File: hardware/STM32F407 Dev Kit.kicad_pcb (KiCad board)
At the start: 4 copper layers, 65.2 x 58.4 mm, 153 parts, among them J1 GMSB0531112YEU, J10 Conn_01x04, J11 TBC 2.54mm 10A, J12 IMP34DT05, J2 Conn_01x06, J3 RJMG1S8008101BR, J4 B2B-XH-A(LF)(SN), J5 Conn_01x04, J7 SJ-3524-SMT, J8 GMSB0531112YEU, J9 Conn_01x04, SW1 SW TACT-SPST, SW2 SW TACT-SPST, SW3 SW TACT-SPST, U1 STM32F103CBT6, U2 DP83826IRHBR, U3 DRV8701ERGET, U4 DMHT6016LFJ-13, U5 ADS122C04IPW, U6 CS43L22, U7 STM32F407VGT6, U8 AP63203WU, U9 XC6206P182MR, Y1 ABM8G-8.000MHZ-18-D2Y-T, Y2 ABM8G-25.000MHZ-9-B4Y-T, Y3 ABM8G-8.000MHZ-18-D2Y-T

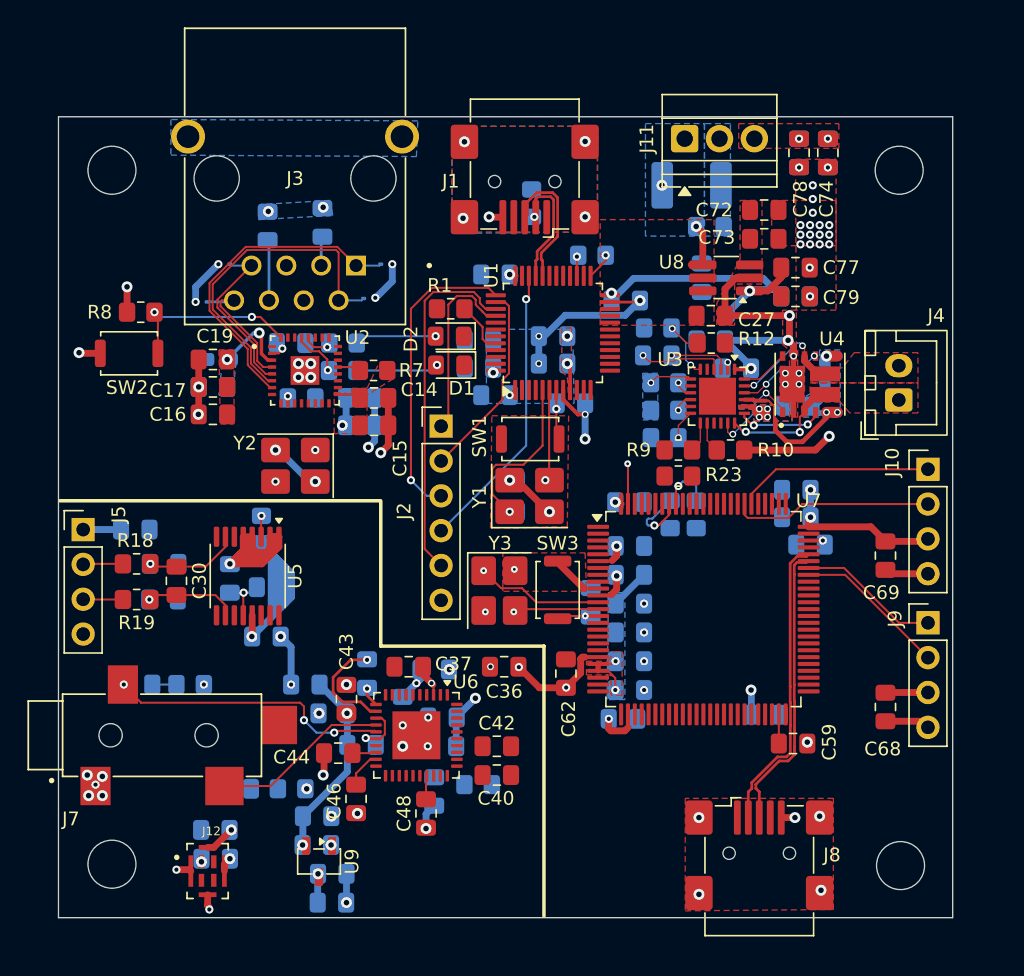
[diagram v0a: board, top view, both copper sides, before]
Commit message: Route Ethernet connections to STM32F407
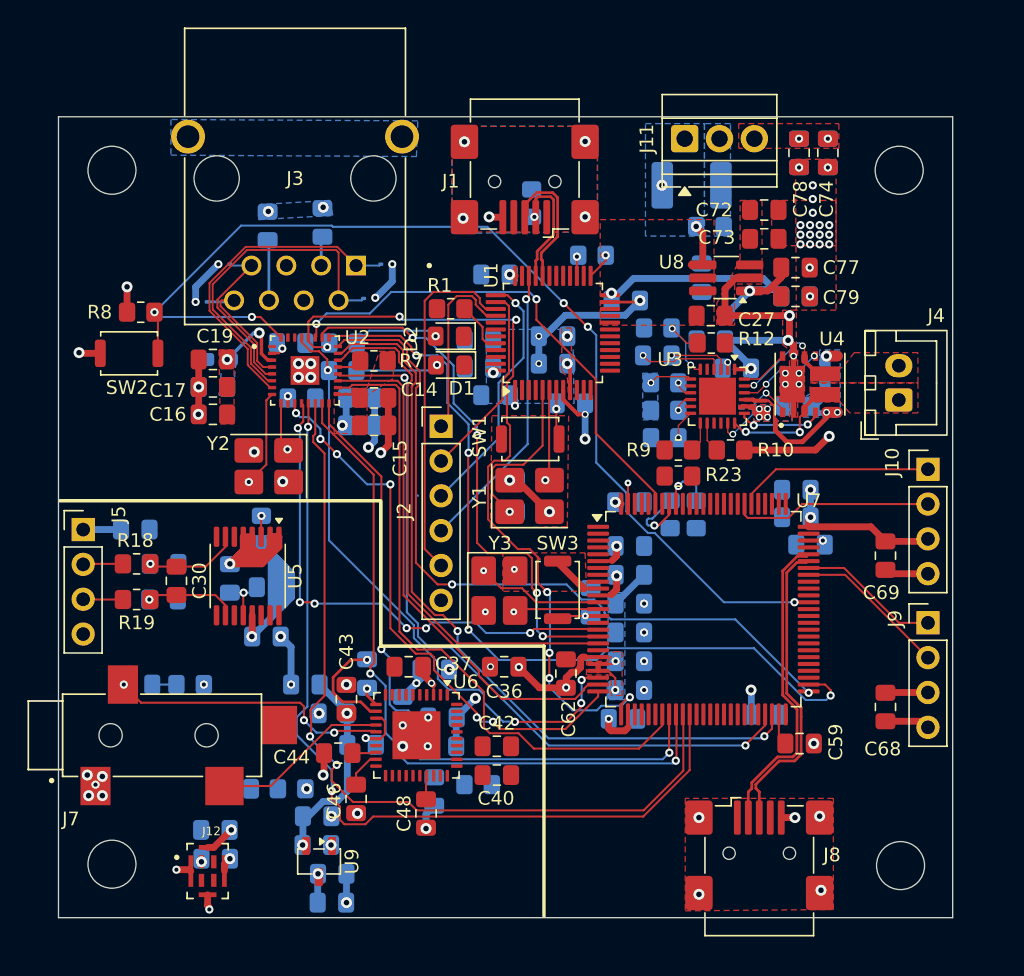
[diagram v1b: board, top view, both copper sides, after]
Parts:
- moved C20 1.95 mm to (165.3, 74.4)
- moved Y2 1.95 mm to (165.3, 75.5)
- moved C21 1.93 mm to (165.3, 76.6)
- moved R7 0.70 mm to (173.0, 67.8)
- moved C59 0.47 mm to (204.0, 95.7)
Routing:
- net PHY_NRST: track 13.1 -> 81.0 mm, vias 2 -> 5
- net RX_D3: track 0.00 -> 63.4 mm, vias 0 -> 2
- net TX_D1: track 0.00 -> 61.2 mm, vias 0 -> 4
- net RX_D2: track 0.00 -> 61.2 mm, vias 0 -> 2
- net COL: track 2.20 -> 58.3 mm, vias 1 -> 7
- net TX_EN: track 0.00 -> 56.1 mm, vias 0 -> 2
- net TX_D0: track 0.00 -> 54.3 mm, vias 0 -> 2
- net RX_ER: track 0.00 -> 54.3 mm, vias 0 -> 2
- net RX_D1: track 0.00 -> 52.4 mm, vias 0 -> 2
- net RX_D0: track 0.00 -> 50.4 mm, vias 0 -> 2
- net RX_DV: track 0.00 -> 48.1 mm
- net CRS: track 3.52 -> 45.1 mm, vias 1 -> 4
- net MDIO: track 0.00 -> 41.0 mm, vias 0 -> 6
- net TX_D2: track 0.00 -> 39.3 mm, vias 0 -> 4
- net TX_CLK: track 0.00 -> 38.5 mm
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
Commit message: Route debugger connections to STM32F407
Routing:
- net F407_JTMS: track 1.54 -> 57.7 mm, vias 1 -> 3
- net F407_JTCLK: track 0.00 -> 50.6 mm, vias 0 -> 2
- net F407_NTRST: track 3.97 -> 27.3 mm, vias 1 -> 3
- net GND: vias 100 -> 99

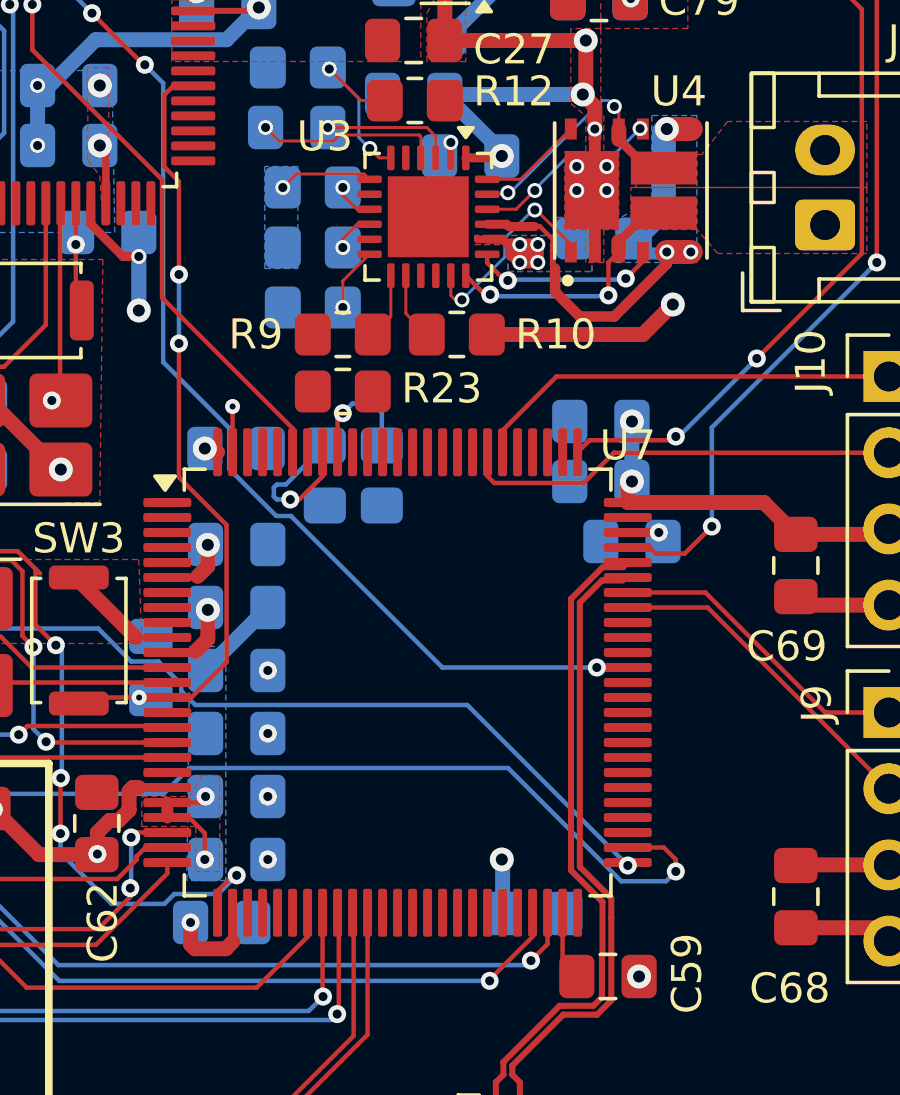
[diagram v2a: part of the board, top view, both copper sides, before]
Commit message: Route Motor connections to STM32F407
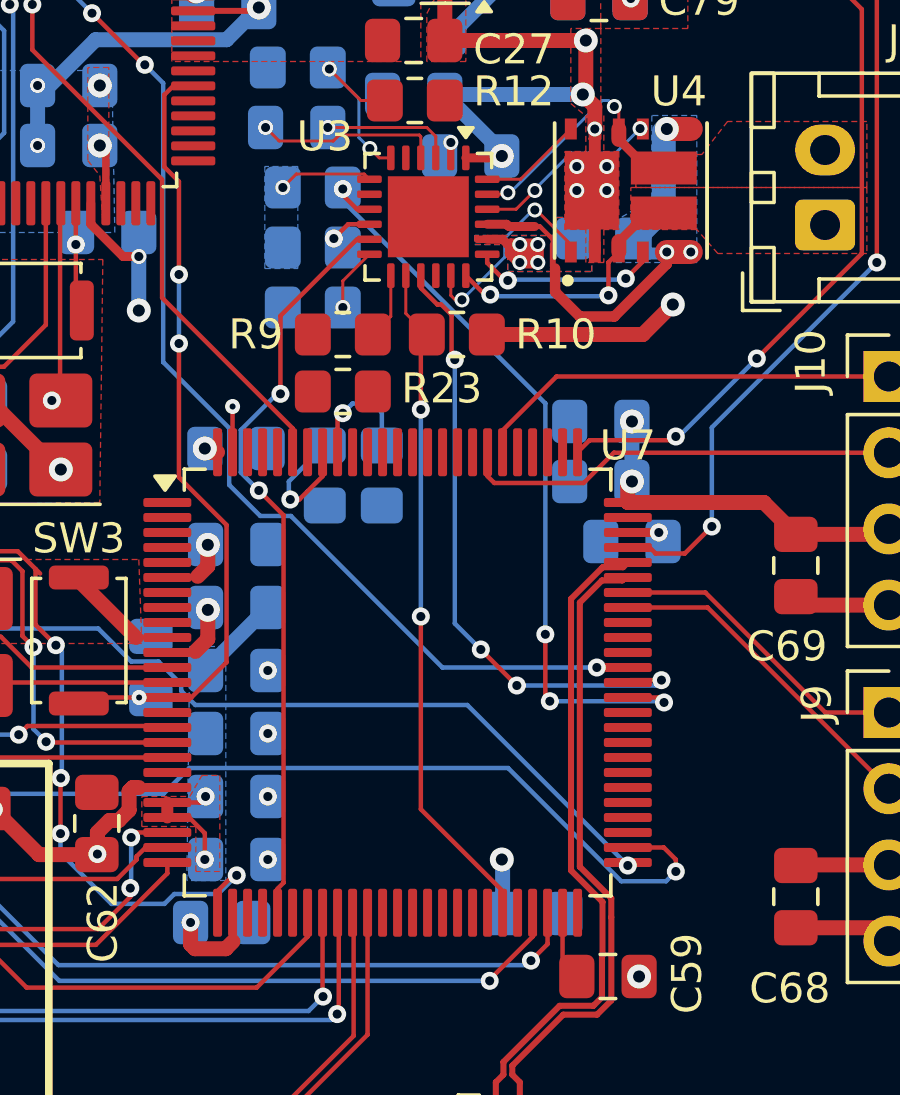
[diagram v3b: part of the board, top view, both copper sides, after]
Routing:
- net SO: track 0.00 -> 25.2 mm, vias 0 -> 2
- net nFAULT: track 1.33 -> 26.4 mm, vias 1 -> 4
- net PH: track 0.00 -> 21.1 mm, vias 0 -> 4
- net EN: track 2.25 -> 22.7 mm, vias 0 -> 2
- net /[8] - STM32F407/SDA: track 5.37 -> 4.51 mm

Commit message: Fix DRC errors
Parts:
- moved C12 2.81 mm to (174.7, 71.4)
- moved C13 2.81 mm to (174.7, 73.4)
- moved C14 2.81 mm to (175.7, 71.4)
- moved C15 2.81 mm to (175.7, 73.4)
- moved C32 2.81 mm to (160.4, 83.5)
- moved C46 2.81 mm to (174.4, 100.6)
- moved C56 2.81 mm to (194.3, 79.0)
- moved C70 2.81 mm to (184.9, 83.9)
- moved D4 2.81 mm to (175.3, 64.2)
- moved D6 2.81 mm to (163.1, 64.4)
- moved R18 2.81 mm to (158.4, 83.5)
- moved R9 2.81 mm to (197.9, 75.2)
- moved D3 2.81 mm to (176.6, 61.6)
- moved C16 2.81 mm to (163.9, 72.6)
- moved C17 2.81 mm to (163.9, 70.6)
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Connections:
- R24 pad 2: /[8] - STM32F407/SCL -> SCL
- R25 pad 1: /[8] - STM32F407/SDA -> SDA
- U7 pad 92: /[8] - STM32F407/SCL -> SCL
- U7 pad 93: /[8] - STM32F407/SDA -> SDA
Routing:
- net GND: track 135.0 -> 226.1 mm, vias 99 -> 119
- net MIC_CLK: track 0.00 -> 81.6 mm, vias 0 -> 2
- net +3V3: track 94.1 -> 162.2 mm, vias 20 -> 36
- net SDA: track 0.00 -> 66.0 mm, vias 0 -> 3
- net MIC_DOUT: track 0.00 -> 61.4 mm, vias 0 -> 2
- net ADC_RST: track 1.54 -> 54.0 mm, vias 1 -> 2
- net SCL: track 0.00 -> 51.2 mm, vias 0 -> 4
- net ADC_DRDY: track 0.00 -> 47.4 mm, vias 0 -> 2
- net CS43L22_SDIN: track 0.00 -> 46.8 mm, vias 0 -> 4
- net CS43L22_LRCK: track 0.00 -> 35.7 mm, vias 0 -> 2
- net CS43L22_RST: track 0.00 -> 30.9 mm, vias 0 -> 2
- net CS43L22_SCLK: track 0.00 -> 26.3 mm, vias 0 -> 4
- net SNSOUT: track 1.81 -> 27.5 mm, vias 1 -> 2
- net SHEILD: track 0.00 -> 24.2 mm
- net +1V8: track 14.8 -> 30.5 mm, vias 2 -> 4
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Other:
- board size 65.2 x 58.4 mm -> 66 x 59.3 mm
